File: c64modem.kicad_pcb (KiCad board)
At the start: 2 copper layers, 47 x 51.2 mm, 27 parts, among them CN1 USERPORT, J1 FTDI_PORT, J2 ESP_01, SW1 UP9600, U1 74LVC125, U2 AZ1117-3.3

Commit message: Reroute
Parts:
- C1, C2, C4, C5, C7: footprint Capacitors_SMD:C_0603_HandSoldering -> Capacitor_SMD:C_0805_2012Metric_Pad1.15x1.40mm_HandSolder
- C3: footprint Capacitors_THT:CP_Radial_D8.0mm_P3.50mm -> Capacitor_THT:CP_Radial_D5.0mm_P2.00mm
- C6: footprint Capacitors_THT:CP_Radial_D5.0mm_P2.00mm -> Capacitor_THT:CP_Radial_D5.0mm_P2.00mm
- C64_RST: renamed from C64 RST; footprint Buttons_Switches_THT:SW_PUSH_6mm -> Button_Switch_THT:SW_PUSH_6mm_H5mm
- D1: value D_Bridge -> D_Bridge_+-AA; footprint Diodes_THT:Diode_Bridge_DIP-4_W7.62mm_P5.08mm -> Package_DIP:DIP-4_W7.62mm_LongPads
- D2, D3, D5: footprint Diodes_THT:D_DO-41_SOD81_P2.54mm_Vertical_AnodeUp -> Diode_THT:D_DO-34_SOD68_P2.54mm_Vertical_AnodeUp
- D4: footprint Diodes_SMD:D_SOD-323 -> Diode_SMD:D_SOD-323
- ESP_PROG: renamed from ESP PROG; footprint Buttons_Switches_THT:SW_PUSH_6mm -> Button_Switch_THT:SW_PUSH_6mm_H5mm
- ESP_RST: renamed from ESP RST; footprint Buttons_Switches_THT:SW_PUSH_6mm -> Button_Switch_THT:SW_PUSH_6mm_H5mm
- J1: footprint Connectors:PINHEAD1-6 -> Connector_PinHeader_2.54mm:PinHeader_1x06_P2.54mm_Vertical
- J2: footprint Pin_Headers:Pin_Header_Straight_2x04_Pitch2.54mm -> Connector_PinSocket_2.54mm:PinSocket_2x04_P2.54mm_Vertical
- JP1: footprint Pin_Headers:Pin_Header_Straight_1x03_Pitch2.54mm -> Connector_PinHeader_2.54mm:PinHeader_1x03_P2.54mm_Vertical
- JP2 RX: renamed from JP2; footprint Pin_Headers:Pin_Header_Straight_1x03_Pitch2.54mm -> Connector_PinHeader_2.54mm:PinHeader_1x03_P2.54mm_Vertical
- R1, R3, R4: footprint Resistors_SMD:R_0603_HandSoldering -> Resistor_SMD:R_0805_2012Metric_Pad1.15x1.40mm_HandSolder
- R2: footprint Resistors_SMD:R_0603_HandSoldering -> Resistor_SMD:R_0805_2012Metric_Pad1.15x1.40mm_HandSolder; moved to F.Cu
- SW1: footprint Buttons_Switches_THT:SW_DIP_x2_W7.62mm_Slide -> Button_Switch_THT:SW_DIP_SPSTx02_Slide_9.78x7.26mm_W7.62mm_P2.54mm
- U1: footprint Housings_SSOP:TSSOP-14_4.4x5mm_Pitch0.65mm -> Package_SO:TSSOP-14_4.4x5mm_P0.65mm
- U2: value AZ1117-3.3 -> AMS1117-3.3; footprint TO_SOT_Packages_SMD:SOT-89-3_Handsoldering -> Package_TO_SOT_SMD:SOT-223
- moved D4 19.9 mm to (137.8, 87.0)
- moved R3 14.9 mm to (139.9, 67.9), turned to 0 degrees
- moved R2 11.6 mm to (135.3, 67.9), turned to 180 degrees
- moved J1 10.7 mm to (129.5, 66.0), turned to 0 degrees
- moved J2 10.7 mm to (141.1, 74.9)
- moved C6 10.4 mm to (167.6, 90.8), turned to 270 degrees
- moved U1 10.1 mm to (150.5, 77.5)
- moved C1 9.83 mm to (170.3, 84.9), turned to 90 degrees
- moved U2 7.87 mm to (164.5, 77.5)
- moved C4 7.64 mm to (160.3, 88.3)
- moved D1 7.37 mm to (144.1, 88.3), turned to 270 degrees
- moved C2 7.24 mm to (163.6, 84.8), turned to 270 degrees
- moved C5 6.38 mm to (160.0, 84.7), turned to 270 degrees
- moved C7 6.00 mm to (166.8, 84.8), turned to 270 degrees
- moved JP2 RX 5.16 mm to (133.0, 83.8), turned to 270 degrees
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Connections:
- net /ESP_DCD renamed Net-(J2-Pad4)
- net /ESP_RST# renamed /~ESP_RST
- CN1 pad 4: Net-(CN1-Pad4) -> (no net)
- CN1 pad 8: Net-(CN1-Pad8) -> (no net)
- CN1 pad 9: Net-(CN1-Pad9) -> (no net)
- CN1 pad E: Net-(CN1-PadE) -> (no net)
- CN1 pad F: Net-(CN1-PadF) -> (no net)
- CN1 pad J: Net-(CN1-PadJ) -> (no net)
- J1 pad 2: Net-(J1-Pad2) -> (no net)
- J1 pad 6: Net-(J1-Pad6) -> (no net)
- J2 pad 2: GND -> /ESP_RX
- J2 pad 8: /ESP_RX -> GND
- U1 pad 10: GND -> /C64_RTS
- U1 pad 14: VCC -> (no net)
- U1 pad 4: /C64_RTS -> GND
- U1 pad 5: GND -> /TX
- U1 pad 6: Net-(J2-Pad6) -> /ESP_RX
- U1 pad 7: GND -> (no net)
- U1 pad 8: /ESP_RX -> Net-(J2-Pad6)
- U1 pad 9: /TX -> GND
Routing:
- net VCC: track 20.4 -> 39.8 mm, vias 1 -> 3
- net /FTDI_TX: track 31.3 -> 12.7 mm
- net /FTDI_RX: track 27.3 -> 11.6 mm
- net /RX: track 14.7 -> 25.9 mm, vias 0 -> 1
- net Net-(J2-Pad4): track 10.2 -> 17.9 mm, vias 1 -> 0
- net Net-(J2-Pad3): track 3.00 -> 10.7 mm, vias 0 -> 1
- net Net-(D1-Pad1): track 2.84 -> 9.95 mm
- net Net-(J2-Pad6): track 26.0 -> 33.0 mm, vias 2 -> 1
- net /~ESP_RST: track 52.1 -> 45.6 mm, vias 0 -> 1
- net /SP2: track 31.0 -> 24.7 mm, vias 1 -> 0
- net GND: track 77.1 -> 71.2 mm, vias 8 -> 4
- net /C64_RTS: track 42.2 -> 36.6 mm, vias 5 -> 3
- net /C64_DCD: track 33.5 -> 38.6 mm, vias 1 -> 3
- net 9VAC2: track 11.2 -> 15.9 mm
- net /SP1: track 27.2 -> 31.8 mm
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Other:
- board size 47 x 51.2 mm -> 47 x 47.5 mm
- board text added: "1"
- board text added: "3.3v"
- board text added: "5V!"
- board text added: "C64Modem v1 JN2020"
- board text added: "ESP8266"
- board text added: "GND"
- board text added: "JLCJLCJLCJLC"
- board text added: "RX"
- board text added: "TX"

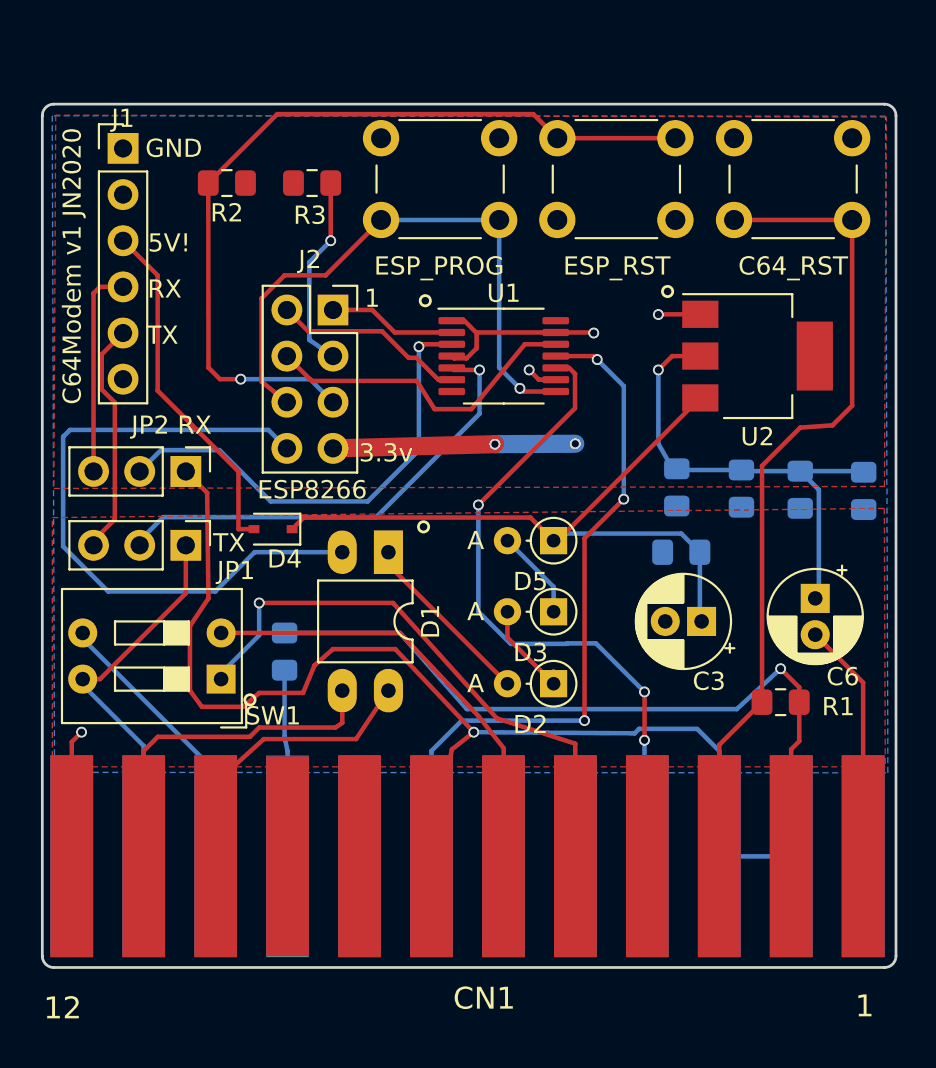
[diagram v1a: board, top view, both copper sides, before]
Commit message: Fixed esp8266 header, routing
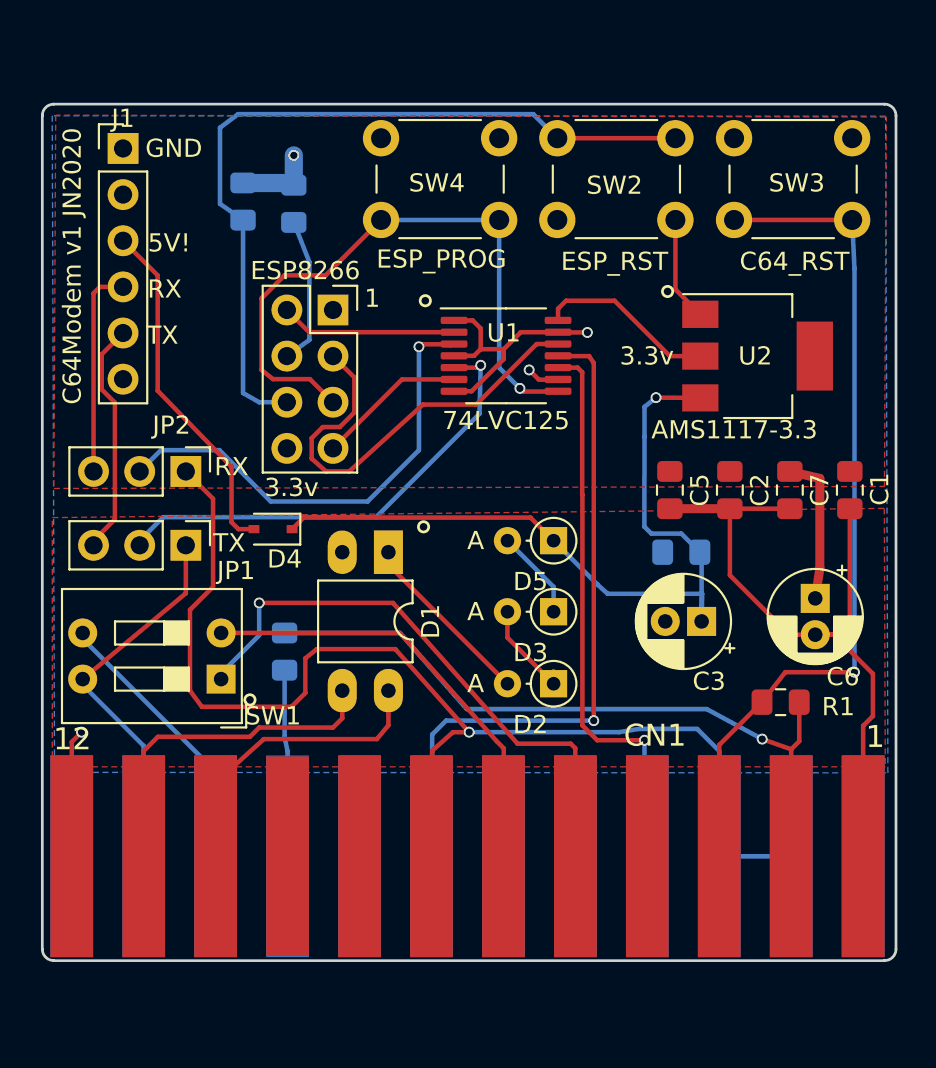
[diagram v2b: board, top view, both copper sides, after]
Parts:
- removed J2: ESP_01, Connector_PinSocket_2.54mm:PinSocket_2x04_P2.54mm_Vertical
- added ESP8266: ESP_01, Connector_PinSocket_2.54mm:PinSocket_2x04_P2.54mm_Vertical, F.Cu at (141.1, 74.9)
- C1, C2, C5, C7: moved to F.Cu
- JP2: renamed from JP2 RX
- R2, R3: moved to B.Cu
- moved R3 1.52 mm to (138.9, 69.1), turned to 270 degrees
- moved R2 1.35 mm to (136.1, 69.0), turned to 270 degrees
- moved C1 0.76 mm to (169.5, 84.8)
- moved C2 0.64 mm to (162.9, 84.8)
- moved C7 0.57 mm to (166.2, 84.8)
- moved C5 0.41 mm to (159.6, 84.8)
- moved U1 0.13 mm to (150.6, 77.5)
- renumbered ESP_RST to SW2, C64_RST to SW3, ESP_PROG to SW4
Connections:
- U1 pad 12: Net-(J2-Pad4) -> /ESP_DCD
- U1 pad 14: (no net) -> VCC
- U1 pad 7: (no net) -> GND
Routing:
- net /ESP_DCD: track 0.00 -> 24.3 mm
- net Net-(J2-Pad4): track 17.9 -> 0.00 mm
- net VCC: track 39.8 -> 22.6 mm, vias 3 -> 1
- net /C64_RTS: track 36.6 -> 31.1 mm, vias 3 -> 1
- net Net-(C3-Pad1): track 39.0 -> 44.2 mm, vias 0 -> 1
- net GND: track 71.2 -> 68.4 mm, vias 4 -> 3
- net /ESP_TX: track 7.09 -> 9.75 mm
- net Net-(ESP8266-Pad4): track 10.7 -> 8.16 mm, vias 1 -> 0
- net /ESP_RX: track 10.7 -> 8.23 mm
- net Net-(ESP8266-Pad5): track 33.0 -> 35.2 mm
- net +5V: track 41.0 -> 39.0 mm
- net /~ESP_RST: track 45.6 -> 43.7 mm, vias 1 -> 0
- net /C64_RX: track 63.9 -> 65.8 mm
- net /RST#: track 45.5 -> 46.8 mm, vias 0 -> 1
- net 9VAC2: track 15.9 -> 16.7 mm
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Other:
- board size 47 x 47.5 mm -> 47 x 47.1 mm
- board text added: "74LVC125"
- board text added: "AMS1117-3.3"
- board text added: "C64_RST"
- board text added: "ESP_PROG"
- board text added: "ESP_RST"
- board text removed: "ESP8266"

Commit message: Rework.
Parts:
- U2: value AMS1117-3.3 -> LDO1117-3.3; footprint Package_TO_SOT_SMD:SOT-223 -> Package_TO_SOT_SMD:SOT-223-3_TabPin2
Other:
- board text added: "LDO-3.3v"
- board text removed: "AMS1117-3.3"

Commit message: Rework & add BOM
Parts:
- C3: footprint Capacitor_THT:CP_Radial_D5.0mm_P2.00mm -> Capacitor_THT:CP_Radial_D10.0mm_P5.00mm
- moved R1 2.18 mm to (167.9, 96.9)
- moved C3 2.10 mm to (163.4, 92.5)
- moved C6 1.89 mm to (168.9, 89.4)
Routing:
- net +5V: track 39.0 -> 36.2 mm
- net Net-(C3-Pad1): track 44.2 -> 45.2 mm
- net VCC: track 22.6 -> 21.6 mm
- net GND: track 68.4 -> 67.6 mm
